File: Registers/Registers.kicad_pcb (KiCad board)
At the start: 2 copper layers, 89.8 x 50.6 mm, 30 parts, among them J1 Conn_01x10_Pin, J2 Conn_01x04_Pin, J3 Conn_01x10_Pin, J4 Conn_01x04_Pin, J5 Conn_01x08_Pin, J6 Conn_01x08_Pin, U1 SN74HCT245N, U2 74LS173, U3 74LS173

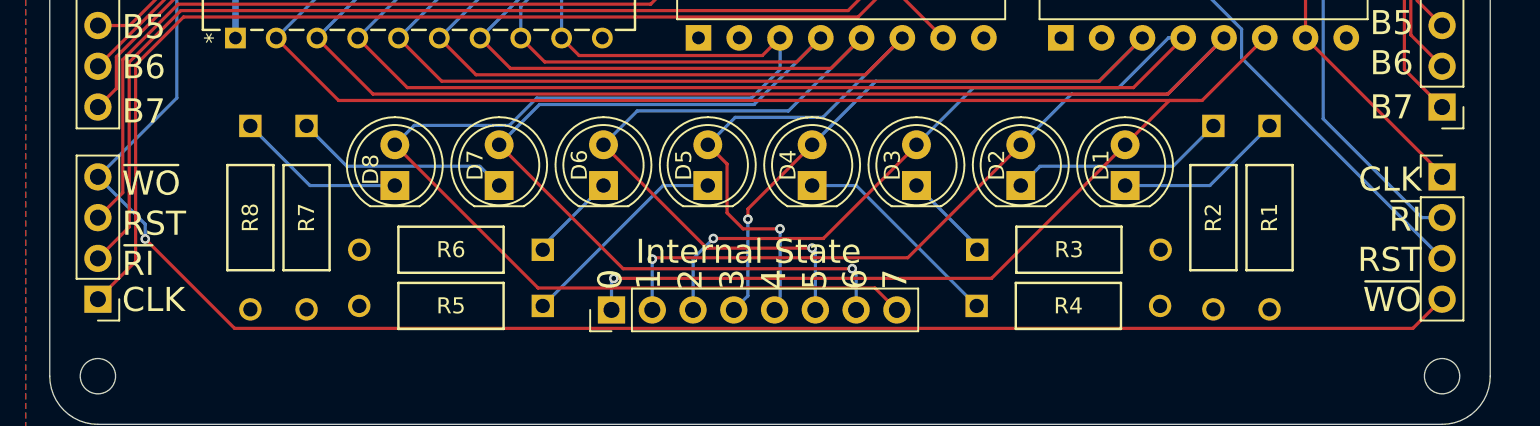
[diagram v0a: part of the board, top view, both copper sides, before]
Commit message: Added pulling resistors to unused pins from bus. (Output 2s comp & B reg write out)
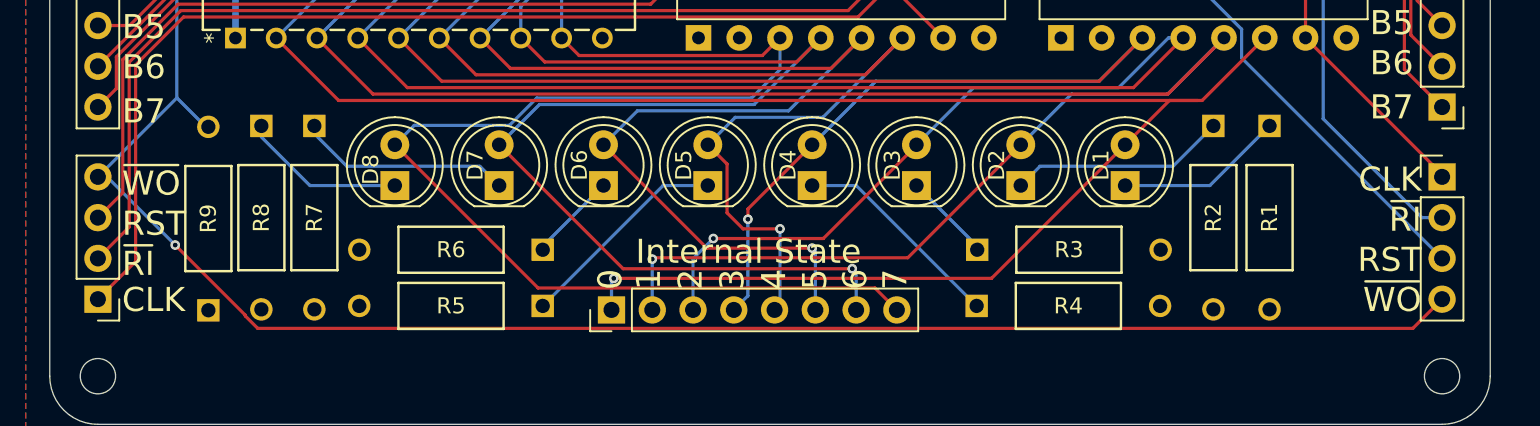
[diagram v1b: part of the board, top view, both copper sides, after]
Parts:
- added R9: 10k, _DownloadFootprints:CF_series_Resistors_THT, F.Cu at (71.9, 80.8)
- moved R8 0.68 mm to (75.2, 69.3)
- moved R7 0.49 mm to (78.5, 69.3)
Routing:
- net /~{WRITE}: track 114.2 -> 116.4 mm
